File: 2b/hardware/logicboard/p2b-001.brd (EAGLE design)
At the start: 91 x 90 mm, 72 parts, among them IC1 74LS06N, IC2 4066N, J1 MKR, J10 1-Wire, J2 GPIO, J3 Vcc, J4** RLY2, J5 SPI, J6 LED, J7 DIN5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

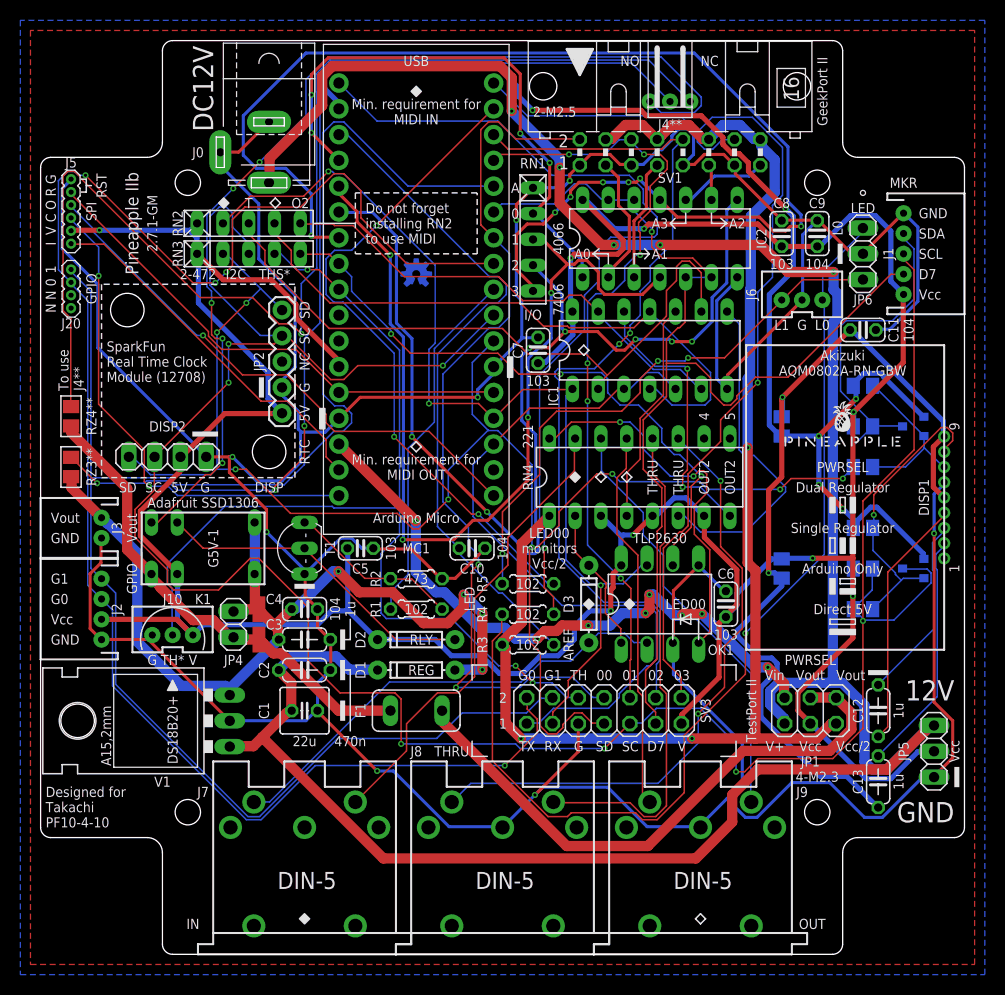
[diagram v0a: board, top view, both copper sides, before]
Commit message: Added RST sw to P2b.
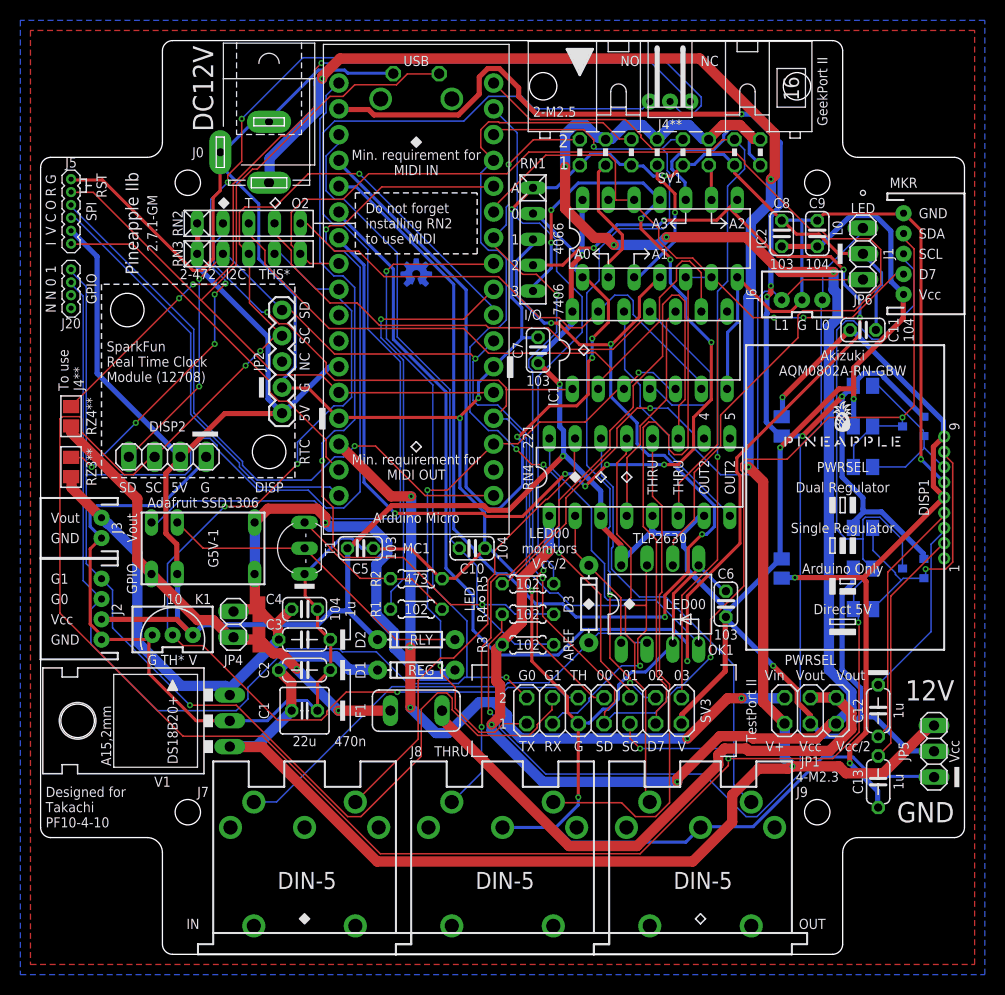
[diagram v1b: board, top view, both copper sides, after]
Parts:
- added S1: RST, switch-omron:B3F-31XX
- J20: value (none) -> GPIO
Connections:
- net GND: now also S1.1
- net RST: now also S1.2
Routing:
- net MNTR: track 61.3 -> 115.9 mm, vias 3 -> 0
- net ANLG2: track 106.9 -> 155.2 mm, vias 7 -> 5
- net RST: track 50.3 -> 87.1 mm
- net RLYOUT2: track 118.8 -> 83.3 mm, vias 1 -> 3
- net VCC/2: track 136.0 -> 169.8 mm, vias 3 -> 7
- net ANLG1: track 92.0 -> 124.6 mm
- net SCL: track 242.0 -> 271.2 mm, vias 7 -> 6
- net ANLG0: track 55.5 -> 80.5 mm, vias 4 -> 3
- net GPIO0: track 166.8 -> 142.8 mm, vias 4 -> 2
- net DTCT0: track 88.3 -> 69.9 mm, vias 2 -> 3
- net V+: track 247.0 -> 230.9 mm, vias 5 -> 4
- net SDA: track 193.9 -> 178.4 mm, vias 8 -> 6
- net ANLG3: track 126.8 -> 112.9 mm, vias 7 -> 10
- net MTRTN: track 61.2 -> 74.9 mm, vias 2 -> 1
- net VCC: track 345.0 -> 332.3 mm, vias 8 -> 6
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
